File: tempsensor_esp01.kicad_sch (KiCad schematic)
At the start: 27 parts, among them J1 Stemma QT, J2 USB_C_Receptacle_USB2.0, SW1 SW_Push, SW2 SW_Push, U1 ESP-01v090, U2 SHT40-AD1B-R2, U3 DPS310, U4 MIC5205-3.3YM5, U5 FT234XD-R

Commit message: complete board
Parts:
- added H1, H2: MountingHole, MountingHole:MountingHole_3.2mm_M3, symbol Mechanical:MountingHole
- C1, C2, C3, C4, C5, C6, C7, C8, C9: footprint (none) -> Capacitor_SMD:C_0402_1005Metric
- R1, R2, R3, R4, R5, R6, R7, R8, R9: footprint (none) -> Resistor_SMD:R_0402_1005Metric
- SW1, SW2: footprint (none) -> ! TS-1187A-B-A-B:SW_Push_SPST_NO_Alps_SKRK
- U5: footprint SON45P300X300X80-13N -> ! FT234XD-R:SON45P300X300X80-13N
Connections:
- net Shield: now reaches J2.S1 (SHIELD), R1.2
- net REG_BP: now reaches C1.1, U4.4 (BP)
- net USBDM renamed FT_USBD-
- net USBDP renamed FT_USBD+
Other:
- moved on the sheet: C1, C2

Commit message: generate out files
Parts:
- C1: LCSC (none) -> C1537
- C2: LCSC (none) -> C12530
- C3, C4: LCSC (none) -> C1567
- C5, C6, C7, C8, C9: LCSC (none) -> C1525
- J1: LCSC (none) -> C160404
- J2: LCSC (none) -> C165948
- R1: LCSC (none) -> C26083
- R2, R3, R4, R5: LCSC (none) -> C25744
- R6, R7: LCSC (none) -> C25905
- R8, R9: LCSC (none) -> C25100
- SW1, SW2: LCSC (none) -> C115357
- U1: LCSC (none) -> C503582
- U2: LCSC (none) -> C2909890
- U3: LCSC (none) -> C130156
- U4: LCSC (none) -> C37970
- U5: LCSC (none) -> C132158
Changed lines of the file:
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@@
+      (effects (font (size 1.27 1.27)) hide)
+    )
+    (property "LCSC" "C165948" (id 4) (at 36.83 54.61 0)
       (effects (font (size 1.27 1.27)) hide)
     )
@@
       (effects (font (size 1.27 1.27)) (justify left bottom) hide)
     )
+    (property "LCSC" "C132158" (id 8) (at 140.97 52.07 0)
+      (effects (font (size 1.27 1.27)) hide)
+    )
     (pin "1")
     (pin "10")
@@
       (effects (font (size 1.27 1.27)) hide)
     )
+    (property "LCSC" "C25905" (id 4) (at 74.93 74.93 0)
+      (effects (font (size 1.27 1.27)) hide)
+    )
     (pin "1")
     (pin "2")
@@
     )
     (property "Datasheet" "~" (id 3) (at 132.08 182.88 0)
+      (effects (font (size 1.27 1.27)) hide)
+    )
+    (property "LCSC" "C1537" (id 4) (at 132.08 182.88 0)
       (effects (font (size 1.27 1.27)) hide)
     )
@@
     (property "PRICE" "None" (id 9) (at 223.52 130.81 0)
       (effects (font (size 1.27 1.27)) (justify left bottom) hide)
+    )
+    (property "LCSC" "C130156" (id 10) (at 223.52 130.81 0)
+      (effects (font (size 1.27 1.27)) hide)
     )
     (pin "1")
@@
       (effects (font (size 1.27 1.27)) hide)
     )
+    (property "LCSC" "C1525" (id 4) (at 144.78 78.74 0)
+      (effects (font (size 1.27 1.27)) hide)
+    )
     (pin "1")
     (pin "2")
@@
     )
     (property "Datasheet" "~" (id 3) (at 39.37 135.89 0)
+      (effects (font (size 1.27 1.27)) hide)
+    )
+    (property "LCSC" "C25744" (id 4) (at 39.37 135.89 0)
       (effects (font (size 1.27 1.27)) hide)
     )
@@
     )
     (property "Datasheet" "~" (id 3) (at 247.65 125.73 0)
+      (effects (font (size 1.27 1.27)) hide)
+    )
+    (property "LCSC" "C1525" (id 4) (at 247.65 125.73 0)
       (effects (font (size 1.27 1.27)) hide)
     )
@@
     )
     (property "Datasheet" "http://l0l.org.uk/2014/12/esp8266-modules-hardware-guide-gotta-catch-em-all/" (id 3) (at 87.63 137.16 0)
+      (effects (font (size 1.27 1.27)) hide)
+    )
+    (property "LCSC" "C503582" (id 4) (at 87.63 137.16 0)
       (effects (font (size 1.27 1.27)) hide)
     )
@@
       (effects (font (size 1.27 1.27)) hide)
     )
+    (property "LCSC" "C115357" (id 4) (at 71.12 175.26 0)
+      (effects (font (size 1.27 1.27)) hide)
+    )
     (pin "1")
     (pin "2")
@@
       (effects (font (size 1.27 1.27)) hide)
     )
+    (property "LCSC" "C25100" (id 4) (at 96.52 40.64 0)
+      (effects (font (size 1.27 1.27)) hide)
+    )
     (pin "1")
     (pin "2")
@@
     )
     (property "Datasheet" "~" (id 3) (at 181.61 130.81 0)
+      (effects (font (size 1.27 1.27)) hide)
+    )
+    (property "LCSC" "C1525" (id 4) (at 181.61 130.81 0)
       (effects (font (size 1.27 1.27)) hide)
     )
@@
       (effects (font (size 1.27 1.27)) (justify left bottom) hide)
     )
+    (property "LCSC" "C2909890" (id 11) (at 163.83 130.81 0)
+      (effects (font (size 1.27 1.27)) hide)
+    )
     (pin "1")
     (pin "2")
@@
       (effects (font (size 1.27 1.27)) hide)
     )
+    (property "LCSC" "C25905" (id 4) (at 74.93 72.39 0)
+      (effects (font (size 1.27 1.27)) hide)
+    )
     (pin "1")
     (pin "2")
@@
     )
     (property "Datasheet" "~" (id 3) (at 90.17 48.26 0)
+      (effects (font (size 1.27 1.27)) hide)
+    )
+    (property "LCSC" "C1567" (id 4) (at 90.17 48.26 0)
       (effects (font (size 1.27 1.27)) hide)
     )
@@
     )
     (property "Datasheet" "~" (id 3) (at 200.66 54.61 0)
+      (effects (font (size 1.27 1.27)) hide)
+    )
+    (property "LCSC" "C160404" (id 4) (at 200.66 54.61 0)
       (effects (font (size 1.27 1.27)) hide)
     )
@@
       (effects (font (size 1.27 1.27)) hide)
     )
+    (property "LCSC" "C1525" (id 4) (at 238.76 125.73 0)
+      (effects (font (size 1.27 1.27)) hide)
+    )
     (pin "1")
     (pin "2")
@@
     )
     (property "Datasheet" "~" (id 3) (at 86.36 48.26 0)
+      (effects (font (size 1.27 1.27)) hide)
+    )
+    (property "LCSC" "C1567" (id 4) (at 86.36 48.26 0)
       (effects (font (size 1.27 1.27)) hide)
     )
@@
       (effects (font (size 1.27 1.27)) hide)
     )
+    (property "LCSC" "C26083" (id 4) (at 33.02 80.01 0)
+      (effects (font (size 1.27 1.27)) hide)
+    )
     (pin "1")
     (pin "2")
@@
       (effects (font (size 1.27 1.27)) hide)
     )
+    (property "LCSC" "C115357" (id 4) (at 38.1 179.07 0)
+      (effects (font (size 1.27 1.27)) hide)
+    )
     (pin "1")
     (pin "2")
@@
       (effects (font (size 1.27 1.27)) hide)
     )
+    (property "LCSC" "C25744" (id 4) (at 237.49 60.96 0)
+      (effects (font (size 1.27 1.27)) hide)
+    )
     (pin "1")
     (pin "2")
@@
       (effects (font (size 1.27 1.27)) hide)
     )
+    (property "LCSC" "C37970" (id 4) (at 118.11 177.8 0)
+      (effects (font (size 1.27 1.27)) hide)
+    )
     (pin "1")
     (pin "2")
@@
       (effects (font (size 1.27 1.27)) hide)
     )
+    (property "LCSC" "C25744" (id 4) (at 46.99 173.99 0)
+      (effects (font (size 1.27 1.27)) hide)
+    )
     (pin "1")
     (pin "2")
@@
       (effects (font (size 1.27 1.27)) hide)
     )
+    (property "LCSC" "C1525" (id 4) (at 133.35 78.74 0)
+      (effects (font (size 1.27 1.27)) hide)
+    )
     (pin "1")
     (pin "2")
@@
     )
     (property "Datasheet" "~" (id 3) (at 135.89 182.88 0)
+      (effects (font (size 1.27 1.27)) hide)
+    )
+    (property "LCSC" "C12530" (id 4) (at 135.89 182.88 0)
       (effects (font (size 1.27 1.27)) hide)
     )
@@
       (effects (font (size 1.27 1.27)) hide)
     )
+    (property "LCSC" "C25100" (id 4) (at 96.52 43.18 0)
+      (effects (font (size 1.27 1.27)) hide)
+    )
     (pin "1")
     (pin "2")
@@
       (effects (font (size 1.27 1.27)) hide)
     )
+    (property "LCSC" "C25744" (id 4) (at 237.49 57.15 0)
+      (effects (font (size 1.27 1.27)) hide)
+    )

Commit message: redesign using CH340E
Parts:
- removed R9: 27R, Resistor_SMD:R_0402_1005Metric, symbol Device:R_Small_US
- removed U5: FT234XD-R, ! FT234XD-R:SON45P300X300X80-13N, symbol ! FT234XD-R-mod:FT234XD-R
- added D1: Red, LED_SMD:LED_0603_1608Metric, symbol Device:LED_Small
- added U5: CH340E, Package_SO:MSOP-10_3x3mm_P0.5mm, symbol Interface_USB:CH340E
- C5, C9: LCSC C1525 -> (none)
- H1, H2: value MountingHole -> M3
- R8: value 27R -> 220R; LCSC C25100 -> (none)
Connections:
- net FT_3V3 is gone; now on net +5V: C9.1
- net +5V: now also U5.7 (VCC); no longer C5.1
- net D+: now also U5.1 (UD+)
- net D-: now also U5.2 (UD-); no longer R8.1
- net GND: now also C5.1, D1.1 (K), U5.3 (GND); no longer C5.2
- net URXD: now also U5.8 (TXD)
- net UTXD: now also U5.9 (RXD)
- net FT_USBD-: no longer names the net of R8.2
- net FT_USBD-: now also D1.2 (A)
- new net: C5.2, U5.10 (V3)
- new net: R8.1, U5.6 (TNOW)
- no-connect marks 7 -> 6
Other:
- moved on the sheet: H1, H2, R6, R7

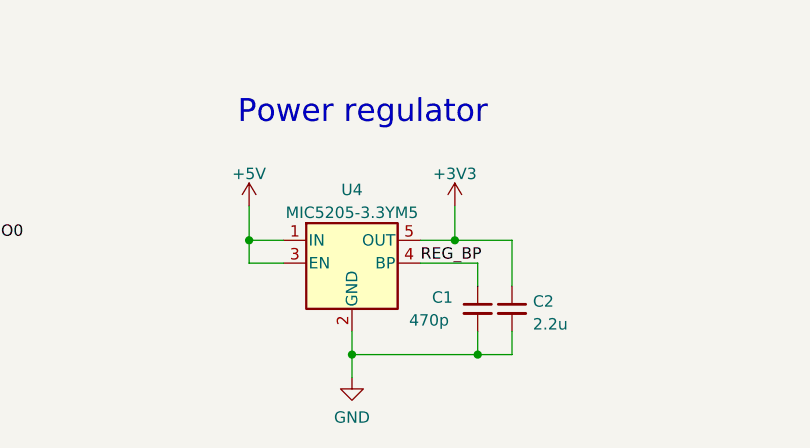
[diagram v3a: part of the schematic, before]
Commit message: change power regulator
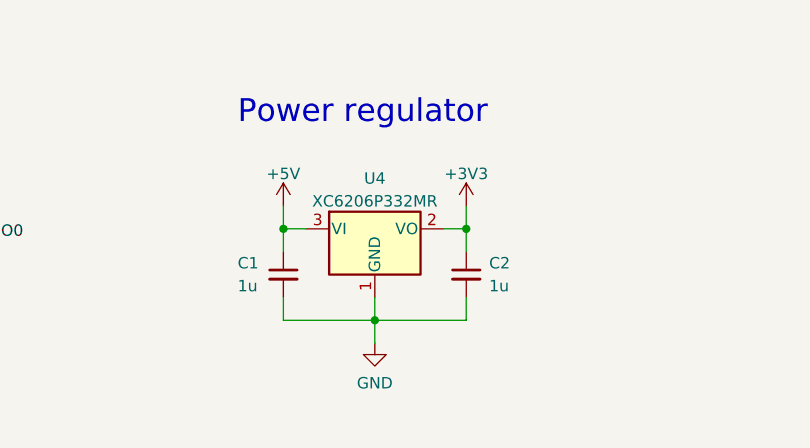
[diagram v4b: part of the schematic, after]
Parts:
- removed U4: MIC5205-3.3YM5, Package_TO_SOT_SMD:SOT-23-5, symbol Regulator_Linear:MIC5205-3.3YM5
- added U4: XC6206P332MR, Package_TO_SOT_SMD:SOT-23, symbol Regulator_Linear:XC6206PxxxMR
- C1: value 470p -> 1u; LCSC C1537 -> C52923
- C2: value 2.2u -> 1u; LCSC C12530 -> C52923
- C5, C9: LCSC (none) -> C1525
- D1: LCSC (none) -> C2286
- R8: LCSC (none) -> C25091
- U5: LCSC (none) -> C99652
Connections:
- net REG_BP is gone; now on net +5V: C1.1
- net +3V3: now also U4.2 (VO)
- net +5V: now also U4.3 (VI)
- net GND: now also U4.1 (GND)
